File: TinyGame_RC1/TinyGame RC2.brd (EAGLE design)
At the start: 38 x 22 mm, 45 parts, among them J1 AUDIO-CONNECTOR-6P-SMD-344003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, K1 BUTTON-4P-3100010P1, K2 BUTTON-4P-3100010P1, K3 BUTTON-4P-3100010P1, K4 BUTTON-4P-3100010P1, U1 MKL02Z32VFK4

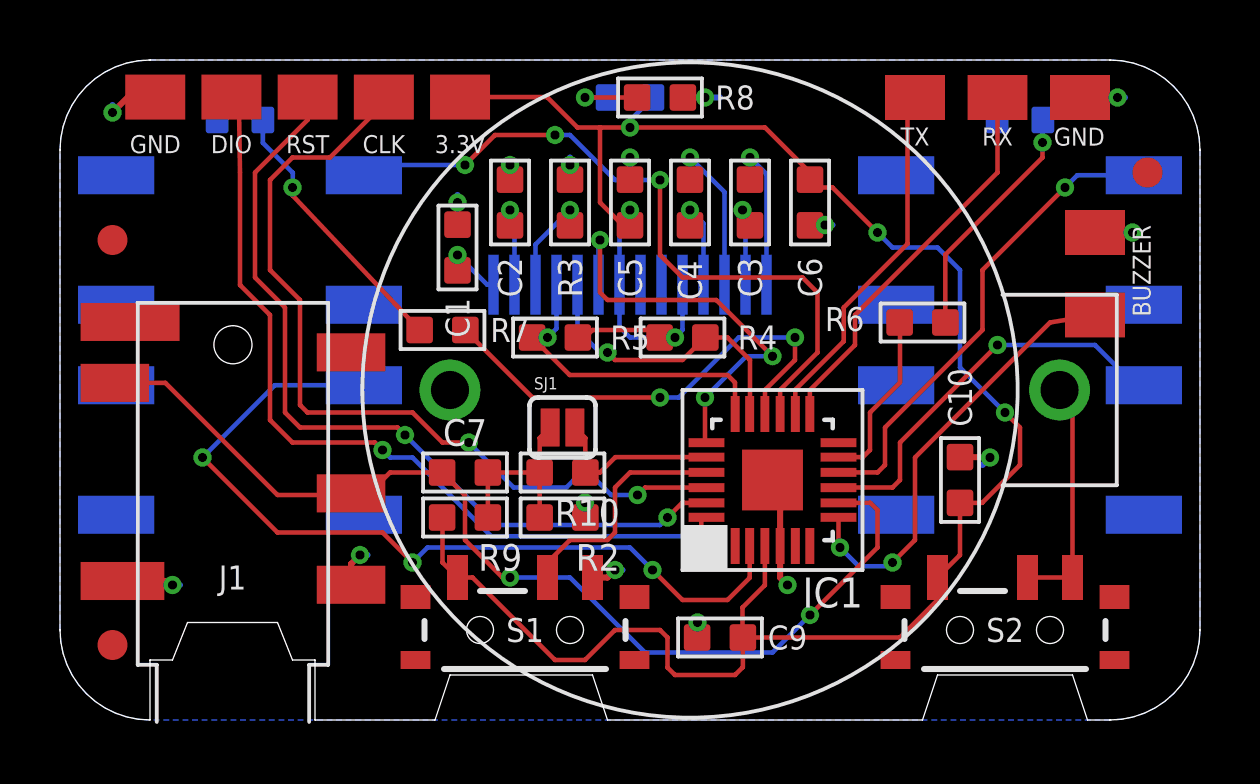
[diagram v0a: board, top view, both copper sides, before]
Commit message: RC2 design update for programming
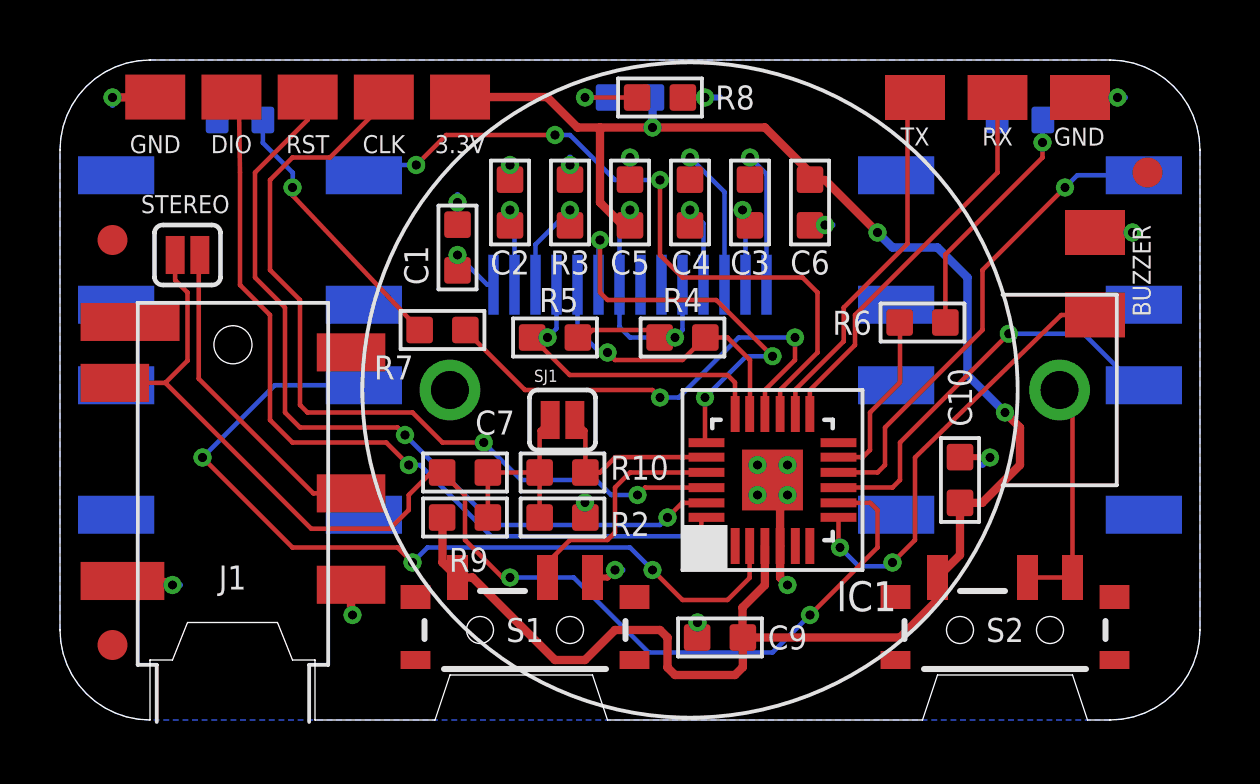
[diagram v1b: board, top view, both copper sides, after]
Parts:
- added STEREO: SOLDERJUMPERNC, SparkFun-Passives:SJ_2S
- R2, R9: value 2K -> 100K
- moved SJ1 0.25 mm to (16.8, 10.0)
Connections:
- net N$20 renamed VBAT
- new net N$1: J1.R, STEREO.1
- net AUDIOHEADPHONE: now also STEREO.2; no longer J1.R
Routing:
- net N$1: track 0.00 -> 10.8 mm
- net AUDIOHEADPHONE: track 34.7 -> 40.7 mm
- net GND: track 20.5 -> 20.2 mm, vias 16 -> 20

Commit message: TinyGame ArtUpdate
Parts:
- added U$5: TINYGAMEARTPOS, TinyGameArt:TINYGAMEART
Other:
- board text removed: "TinyGame"

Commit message: Artwork and gerbers
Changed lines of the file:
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@@
 <grid distance="0.01" unitdist="mm" unit="mm" style="lines" multiple="1" display="yes" altdistance="0.025" altunitdist="inch" altunit="inch"/>
 <layers>
-<layer number="1" name="Top" color="4" fill="1" visible="no" active="yes"/>
+<layer number="1" name="Top" color="4" fill="1" visible="yes" active="yes"/>
 <layer number="2" name="Route2" color="1" fill="3" visible="no" active="no"/>
 <layer number="3" name="Route3" color="4" fill="3" visible="no" active="no"/>
@@
 <layer number="15" name="Route15" color="4" fill="6" visible="no" active="no"/>
 <layer number="16" name="Bottom" color="1" fill="1" visible="no" active="yes"/>
-<layer number="17" name="Pads" color="2" fill="1" visible="no" active="yes"/>
-<layer number="18" name="Vias" color="2" fill="1" visible="no" active="yes"/>
+<layer number="17" name="Pads" color="2" fill="1" visible="yes" active="yes"/>
+<layer number="18" name="Vias" color="2" fill="1" visible="yes" active="yes"/>
 <layer number="19" name="Unrouted" color="6" fill="1" visible="no" active="yes"/>
-<layer number="20" name="Dimension" color="15" fill="1" visible="yes" active="yes"/>
-<layer number="21" name="tPlace" color="7" fill="1" visible="no" active="yes"/>
-<layer number="22" name="bPlace" color="7" fill="1" visible="yes" active="yes"/>
+<layer number="20" name="Dimension" color="15" fill="1" visible="no" active="yes"/>
+<layer number="21" name="tPlace" color="7" fill="1" visible="yes" active="yes"/>
+<layer number="22" name="bPlace" color="7" fill="1" visible="no" active="yes"/>
 <layer number="23" name="tOrigins" color="15" fill="1" visible="no" active="yes"/>
-<layer number="24" name="bOrigins" color="15" fill="1" visible="yes" active="yes"/>
-<layer number="25" name="tNames" color="7" fill="1" visible="no" active="yes"/>
+<layer number="24" name="bOrigins" color="15" fill="1" visible="no" active="yes"/>
+<layer number="25" name="tNames" color="7" fill="1" visible="yes" active="yes"/>
 <layer number="26" name="bNames" color="7" fill="1" visible="no" active="yes"/>
 <layer number="27" name="tValues" color="7" fill="1" visible="no" active="yes"/>
@@
 <wire x1="35" y1="0" x2="38" y2="3" width="0" layer="20" curve="90"/>
 <text x="31.25" y="19.75" size="0.6" layer="21" rot="R180" align="bottom-center">RX</text>
-<text x="28.5" y="19.75" size="0.6" layer="21" rot="R180" align="bottom-center">TX</text>
+<text x="28.92" y="19.75" size="0.6" layer="21" rot="R180" align="bottom-center">TX</text>
 <text x="33.975" y="19.745" size="0.6" layer="21" rot="R180" align="bottom-center">GND</text>
 <text x="13.335" y="19.495" size="0.6" layer="21" rot="R180" align="bottom-center">3.3V</text>
@@
 </element>
 <element name="R7" library="OPL" package="R0603" value="2K" x="12.75" y="13" smashed="yes">
-<attribute name="NAME" x="11.125" y="11.75" size="0.8" layer="25" ratio="11" align="center"/>
+<attribute name="NAME" x="11.185" y="11" size="0.8" layer="25" ratio="11" align="center"/>
 </element>
 <element name="R8" library="OPL" package="R0603" value="2K" x="20" y="20.75" smashed="yes" rot="R180">
@@
 </element>
 <element name="R9" library="OPL" package="R0603" value="100K" x="13.5" y="6.75" smashed="yes" rot="R180">
-<attribute name="NAME" x="14.28" y="5.74" size="0.8" layer="25" ratio="11" rot="R180"/>
+<attribute name="NAME" x="15.1" y="5.94" size="0.8" layer="25" ratio="11" rot="R180"/>
 </element>
 <element name="R10" library="OPL" package="R0603" value="2K" x="16.75" y="8.25" smashed="yes" rot="R180">
